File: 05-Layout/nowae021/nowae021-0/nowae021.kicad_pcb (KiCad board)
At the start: 2 copper layers, 25.4 x 25.4 mm, 37 parts, among them P1 NVT_BUS, P2 NVT_BUS, Q1 PDTC123EU, Q2 PDTC123EU, Q3 PDTC123EU, Q4 PDTC123EU, Q5 PDTC123EU, Q6 PDTC123EU, SW1 BUTTON-WE_434153017835, U1 MKL15Z128VFM4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

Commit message: WiP routing (nowae021-0)
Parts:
- DL1, DL2, DL3, DL4, DL5, DL6, Q1, Q2, Q3, Q4, Q5, Q6, R1, R2, R3, R4, R5, R6: moved to B.Cu
- moved R9 77.2 mm to (105.7, 73.4)
- moved C7 76.7 mm to (105.7, 75.0), turned to 180 degrees
- moved R8 76.1 mm to (107.7, 86.7)
- moved C3 73.0 mm to (110.7, 76.6), turned to 180 degrees
- moved R7 70.1 mm to (116.6, 86.6), turned to 180 degrees
- moved C2 70.0 mm to (110.7, 74.8), turned to 180 degrees
- moved R11 62.2 mm to (120.0, 88.0), turned to 180 degrees
- moved C4 60.8 mm to (119.9, 83.8), turned to 180 degrees
- moved DL7 58.4 mm to (120.0, 89.6), turned to 180 degrees
- moved C1 49.6 mm to (120.0, 77.8), turned to 180 degrees
- moved Q6 28.6 mm to (120.0, 85.8), turned to 270 degrees
- moved R10 28.4 mm to (104.9, 86.7), turned to 180 degrees
- moved Q5 28.4 mm to (120.0, 81.4), turned to 270 degrees
- moved SW1 28.3 mm to (104.9, 84.2)
- moved Q4 28.2 mm to (120.0, 77.0), turned to 270 degrees
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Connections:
- U1 pad 25: /FIRE_LED4 -> /FIRE_LED6
- U1 pad 30: /FIRE_LED6 -> /FIRE_LED4
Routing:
- net +VIN: track 0.00 -> 28.5 mm
- net /FIRE_LED5: track 0.00 -> 17.7 mm, vias 0 -> 1
- net /FIRE_LED4: track 0.00 -> 15.8 mm, vias 0 -> 1
- net /FIRE_LED6: track 0.00 -> 15.7 mm, vias 0 -> 1
- net GND: track 0.00 -> 14.1 mm
- net /FIRE_LED1: track 0.00 -> 12.7 mm, vias 0 -> 1
- net /FIRE_LED2: track 0.00 -> 8.78 mm, vias 0 -> 1
- net /FIRE_LED3: track 0.00 -> 8.18 mm, vias 0 -> 1
- net Net-(C5-Pad1): track 0.00 -> 5.89 mm
- net +3.3V: track 0.00 -> 5.80 mm
- net Net-(C6-Pad1): track 0.00 -> 5.77 mm
- net Net-(DL5-Pad1): track 0.00 -> 5.66 mm
- net Net-(DL1-Pad1): track 0.00 -> 5.66 mm
- net Net-(DL6-Pad1): track 0.00 -> 5.66 mm
- net Net-(DL2-Pad1): track 0.00 -> 5.66 mm
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- added copper zone on B.Cu, net GND
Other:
- board size 25.4 x 25.4 mm -> 20.3 x 20.3 mm
- net class Default: trace_width 0.25 -> 0.2
- rule via_min_size: 0.4 -> 0.6

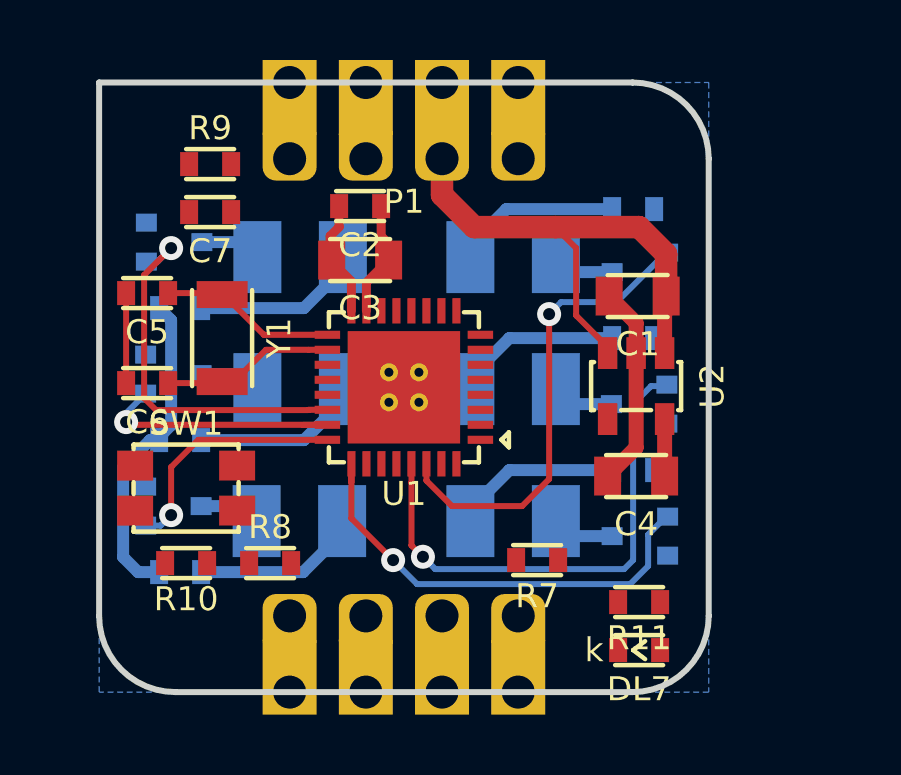
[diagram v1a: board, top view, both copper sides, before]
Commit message: WiP routing... is very hard with only two layer!
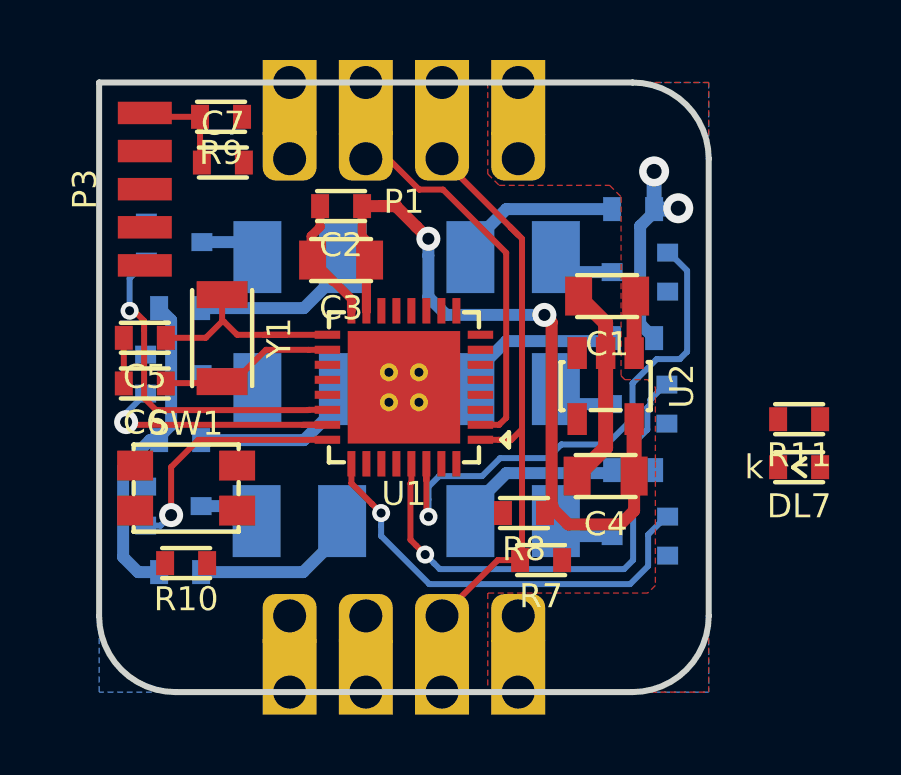
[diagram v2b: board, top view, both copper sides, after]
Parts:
- added P3: SWD, CONNECTOR:CONN-PAD-5x1-1.27, F.Cu at (103.5, 74.2)
- moved R8 8.63 mm to (116.2, 85.0), turned to 180 degrees
- moved R11 8.10 mm to (125.3, 81.9)
- moved DL7 8.10 mm to (125.3, 83.5)
- moved C7 1.71 mm to (106.1, 73.3), turned to 0 degrees
- moved R9 1.62 mm to (106.1, 71.8), turned to 180 degrees
- moved C5 1.49 mm to (103.5, 79.2)
- moved C1 1.02 mm to (118.9, 77.8)
- moved C4 1.02 mm to (118.9, 83.8)
- moved U2 1.02 mm to (118.9, 80.8)
- moved C2 0.64 mm to (110.1, 74.8)
- moved C3 0.64 mm to (110.1, 76.6)
- moved R7 0.13 mm to (116.7, 86.6)
- moved C6 0.08 mm to (103.5, 80.7)
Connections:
- P1 pad 1: /NTV_COMM_SDA -> +VIN
- P1 pad 2: +VIN -> /NTV_COMM_SDA
- P1 pad 3: GND -> /NTV_COMM_SCL
- P1 pad 4: /NTV_COMM_SCL -> GND
- P2 pad 1: /NTV_COMM_SDA -> +VIN
- P2 pad 2: +VIN -> /NTV_COMM_SDA
- P2 pad 3: GND -> /NTV_COMM_SCL
- P2 pad 4: /NTV_COMM_SCL -> GND
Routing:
- net +3.3V: track 5.80 -> 26.9 mm, vias 0 -> 2
- net /NTV_COMM_SDA: track 0.00 -> 19.8 mm
- net /NTV_COMM_SCL: track 0.00 -> 12.6 mm
- net +VIN: track 28.5 -> 20.0 mm, vias 0 -> 2
- net /RESET: track 0.00 -> 3.44 mm
- net /FIRE_LED4: track 15.8 -> 18.3 mm
- net Net-(C5-Pad1): track 5.89 -> 7.54 mm
- net /FIRE_LED1: track 12.7 -> 11.3 mm
- net /FIRE_LED6: track 15.7 -> 14.8 mm
- net /FIRE_LED5: track 17.7 -> 17.0 mm
- added copper zone on F.Cu, net +VIN
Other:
- net class Default: via_dia 0.8 -> 0.6; via_drill 0.4 -> 0.3

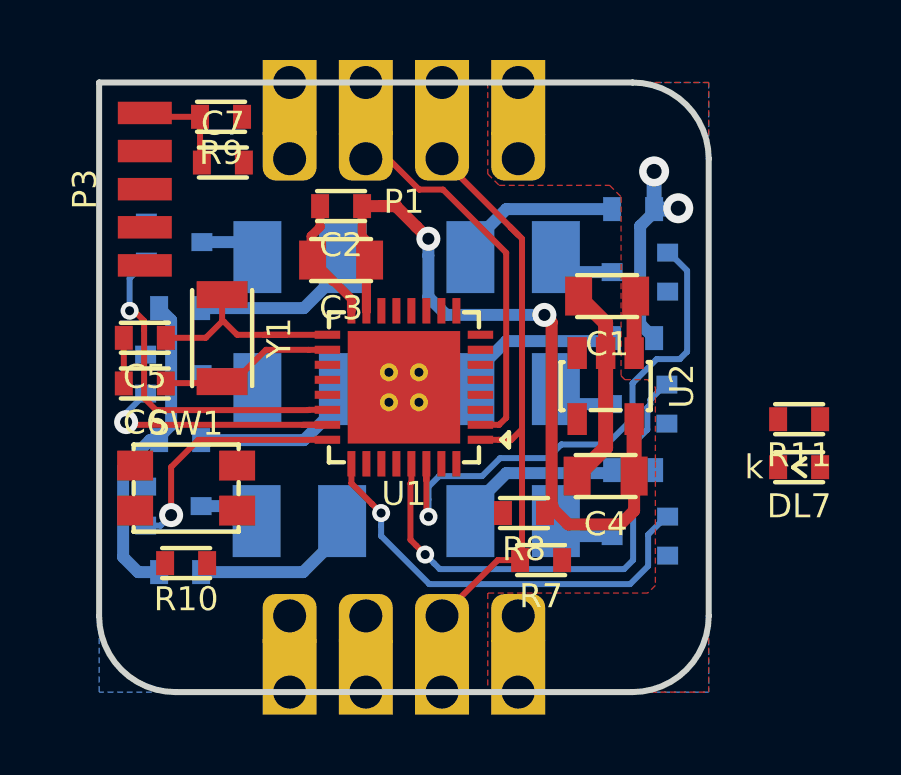
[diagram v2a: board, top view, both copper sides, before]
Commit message: Deleted debug connector. Wip routing.
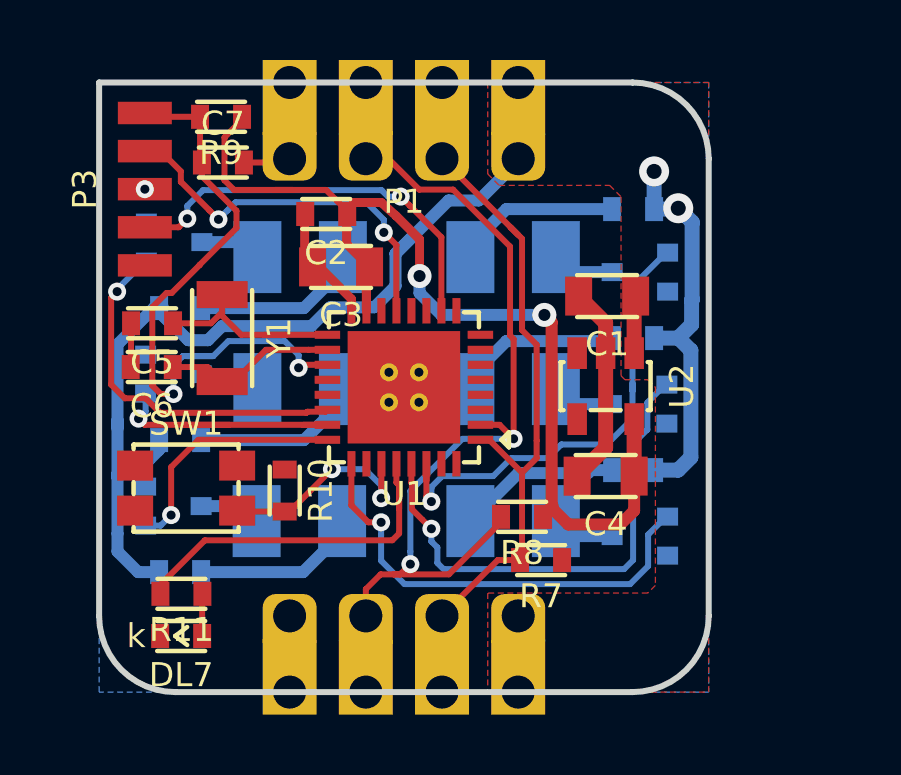
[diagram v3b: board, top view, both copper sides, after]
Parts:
- moved R11 21.4 mm to (104.7, 87.7)
- moved DL7 21.4 mm to (104.7, 89.1)
- moved R10 4.08 mm to (108.2, 84.3), turned to 270 degrees
- moved C6 0.59 mm to (103.8, 80.2)
- moved C2 0.56 mm to (109.6, 75.1)
- moved C5 0.54 mm to (103.8, 78.7)
- moved C3 0.23 mm to (110.1, 76.8)
- moved R8 0.14 mm to (116.1, 85.2)
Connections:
- net /DEBUG_RX renamed Net-(U1-Pad4)
- net /DEBUG_TX renamed Net-(U1-Pad3)
- U1 pad 21: /MCU_STATUS -> Net-(U1-Pad21)
- U1 pad 27: Net-(U1-Pad27) -> /ADDR_PROG
- U1 pad 28: /ADDR_PROG -> /MCU_STATUS
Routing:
- net +VIN: track 20.0 -> 49.5 mm
- net /NTV_COMM_SCL: track 12.6 -> 31.2 mm, vias 0 -> 2
- net /RESET: track 3.44 -> 21.4 mm, vias 0 -> 2
- net /SWCLK: track 0.00 -> 13.7 mm, vias 0 -> 2
- net /SWDIO: track 0.00 -> 12.8 mm, vias 0 -> 2
- net /MCU_STATUS: track 0.00 -> 11.8 mm
- net +3.3V: track 26.9 -> 35.5 mm
- net /ADDR_PROG: track 0.00 -> 7.20 mm, vias 0 -> 2
- net /NTV_COMM_SDA: track 19.8 -> 24.5 mm
- net GND: track 13.9 -> 18.1 mm, vias 0 -> 1
- net /FIRE_LED4: track 18.3 -> 16.5 mm
- net Net-(DL7-Pad1): track 0.00 -> 1.60 mm
- net /FIRE_LED1: track 11.3 -> 12.3 mm
- net /FIRE_LED2: track 8.78 -> 9.65 mm
- net /FIRE_LED6: track 14.8 -> 15.5 mm

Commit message: WiP routing (nowae021-0)
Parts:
- moved Y1 0.62 mm to (106.7, 79.4)
- moved C6 0.62 mm to (104.4, 80.1)
- moved C5 0.57 mm to (104.3, 78.7)
- moved P3 0.30 mm to (103.2, 74.2)
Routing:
- net GND: track 18.1 -> 31.7 mm, vias 1 -> 2
- net +3.3V: track 35.5 -> 43.8 mm, vias 2 -> 4
- net /RESET: track 21.4 -> 20.2 mm
- net Net-(C5-Pad1): track 7.12 -> 8.24 mm

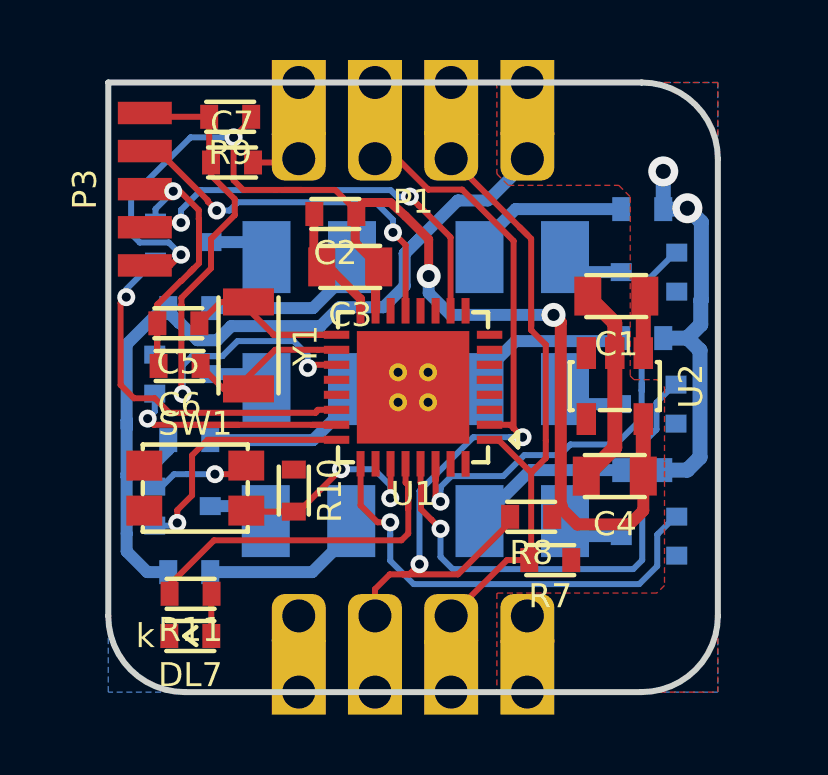
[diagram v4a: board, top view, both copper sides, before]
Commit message: Added 2.54mm on width. WiP routing.
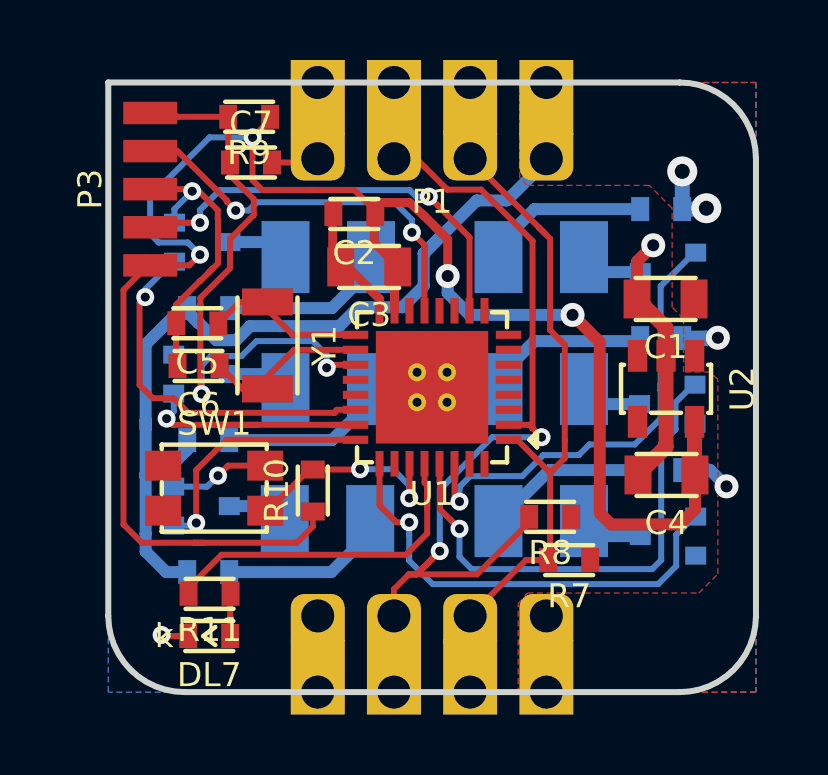
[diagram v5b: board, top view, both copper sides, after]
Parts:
- moved C4 1.72 mm to (120.6, 83.8)
- moved U2 1.71 mm to (120.6, 80.9)
- moved C1 1.65 mm to (120.6, 77.9)
- moved C2 0.63 mm to (110.2, 75.1)
- moved C3 0.63 mm to (110.7, 76.8)
- moved C5 0.63 mm to (105.0, 78.7)
- moved DL3 0.63 mm to (109.3, 85.3)
- moved DL4 0.63 mm to (116.4, 76.5)
- moved DL5 0.63 mm to (116.4, 80.9)
- moved DL6 0.63 mm to (116.4, 85.3)
- moved P1 0.63 mm to (112.8, 72.0)
- moved P2 0.63 mm to (112.8, 89.7)
- moved Q2 0.63 mm to (105.1, 80.4)
- moved Q3 0.63 mm to (105.1, 84.8)
- moved R10 0.63 mm to (108.8, 84.3), turned to 90 degrees
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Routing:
- net +3.3V: track 43.8 -> 61.7 mm
- net +VIN: track 49.5 -> 39.8 mm, vias 2 -> 4
- net GND: track 31.7 -> 39.3 mm, vias 2 -> 4
- net /NTV_COMM_SCL: track 30.7 -> 31.8 mm
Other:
- board size 20.3 x 20.3 mm -> 21.6 x 20.3 mm

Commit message: WiP routing (nowae021-0)
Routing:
- net GND: track 39.3 -> 43.9 mm, vias 4 -> 6
- net +3.3V: track 61.7 -> 65.6 mm

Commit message: Routing ended! (nowae021-0)
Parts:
- added G***: LOGO, LOGO:LOGO_NOWAE_10MM_FSILK, F.Cu at (117.1, 79.5)
- moved R9 1.50 mm to (106.7, 73.3)
- moved C7 1.50 mm to (106.8, 71.8)
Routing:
- net GND: track 43.9 -> 59.3 mm, vias 6 -> 7
- net +VIN: track 40.0 -> 50.2 mm
- net +3.3V: track 65.6 -> 73.0 mm
- net /ADDR_PROG: track 7.21 -> 10.6 mm
